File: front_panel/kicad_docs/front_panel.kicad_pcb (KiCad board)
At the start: 2 copper layers, 60.6 x 128.5 mm, 4 parts

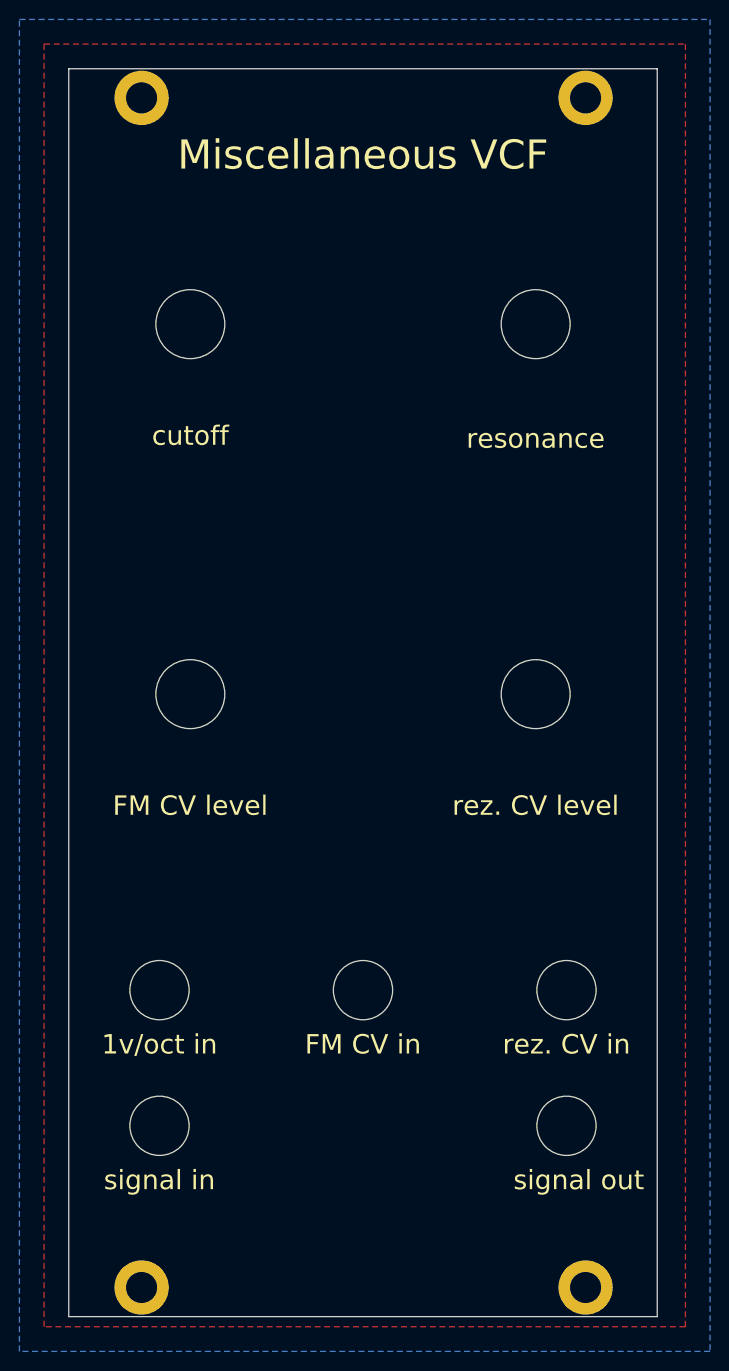
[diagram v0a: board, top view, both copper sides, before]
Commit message: fix misplaced headers, update readme
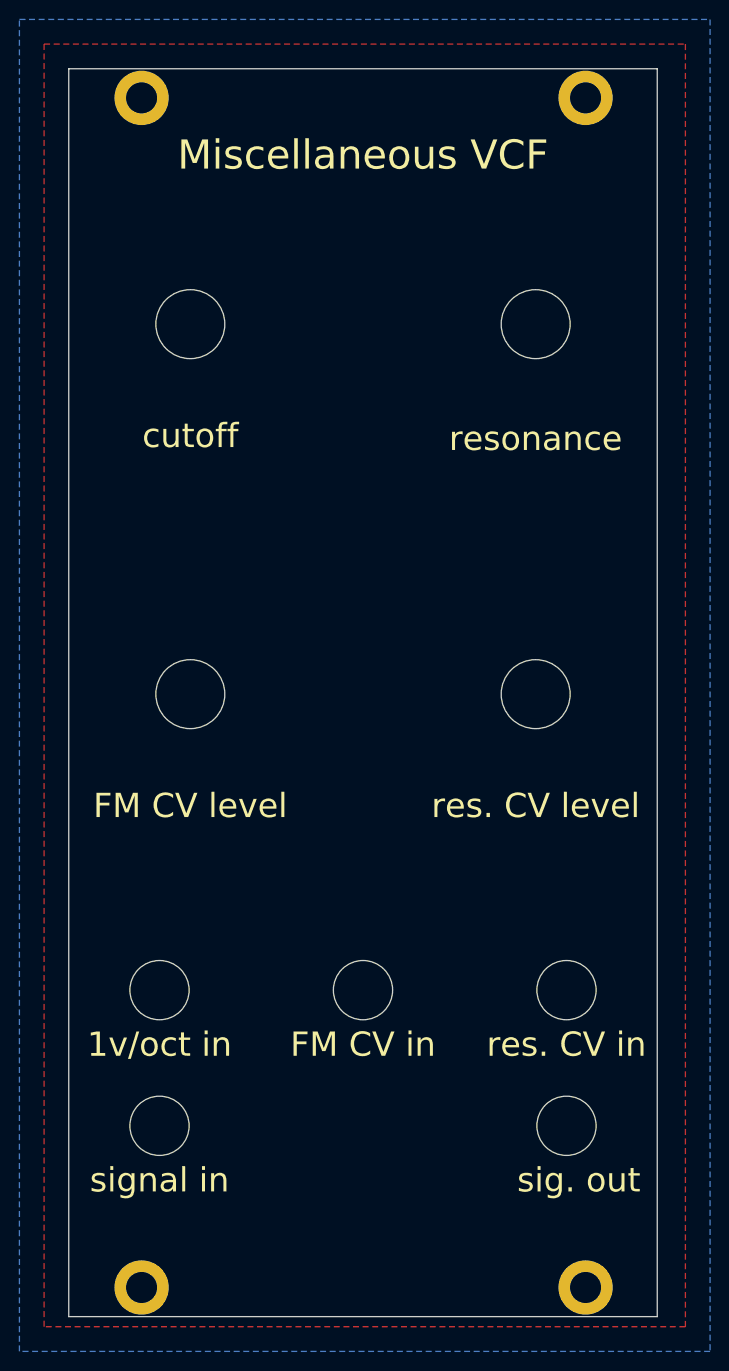
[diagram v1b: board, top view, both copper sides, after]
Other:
- board text added: "res. CV in"
- board text added: "res. CV level"
- board text added: "sig. out"
- board text removed: "rez. CV in"
- board text removed: "rez. CV level"
- board text removed: "signal out"
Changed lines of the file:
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@@
     (visible_elements FFFFFF7F)
     (pcbplotparams
-      (layerselection 0x010fc_ffffffff)
+      (layerselection 0x010f0_ffffffff)
       (usegerberextensions false)
       (usegerberattributes true)
       (usegerberadvancedattributes true)
-      (creategerberjobfile true)
+      (creategerberjobfile false)
       (excludeedgelayer true)
       (linewidth 0.100000)
@@
       (outputformat 1)
       (mirror false)
-      (drillshape 1)
+      (drillshape 0)
       (scaleselection 1)
-      (outputdirectory ""))
+      (outputdirectory "../construction_docs/gerbers/"))
   )
   (net 0 "")
@@
       (effects (font (size 1 1) (thickness 0.15)))
     )
+    (fp_circle (center 0 0) (end 2.8 0) (layer Cmts.User) (width 0.15))
+    (fp_circle (center 0 0) (end 3.05 0) (layer F.CrtYd) (width 0.05))
     (fp_text user %R (at 0.3 0) (layer F.Fab)
       (effects (font (size 1 1) (thickness 0.15)))
     )
-    (fp_circle (center 0 0) (end 2.8 0) (layer Cmts.User) (width 0.15))
-    (fp_circle (center 0 0) (end 3.05 0) (layer F.CrtYd) (width 0.05))
     (pad 1 thru_hole circle (at 0 0) (size 5.6 5.6) (drill 3.2) (layers *.Cu *.Mask)
       (net 1 GND))
@@
       (effects (font (size 1 1) (thickness 0.15)))
     )
+    (fp_circle (center 0 0) (end 2.8 0) (layer Cmts.User) (width 0.15))
+    (fp_circle (center 0 0) (end 3.05 0) (layer F.CrtYd) (width 0.05))
     (fp_text user %R (at 0.3 0) (layer F.Fab)
       (effects (font (size 1 1) (thickness 0.15)))
     )
-    (fp_circle (center 0 0) (end 2.8 0) (layer Cmts.User) (width 0.15))
-    (fp_circle (center 0 0) (end 3.05 0) (layer F.CrtYd) (width 0.05))
     (pad 1 thru_hole circle (at 0 0) (size 5.6 5.6) (drill 3.2) (layers *.Cu *.Mask)
       (net 1 GND))
@@
       (effects (font (size 1 1) (thickness 0.15)))
     )
+    (fp_circle (center 0 0) (end 2.8 0) (layer Cmts.User) (width 0.15))
+    (fp_circle (center 0 0) (end 3.05 0) (layer F.CrtYd) (width 0.05))
     (fp_text user %R (at 0.3 0) (layer F.Fab)
       (effects (font (size 1 1) (thickness 0.15)))
     )
-    (fp_circle (center 0 0) (end 2.8 0) (layer Cmts.User) (width 0.15))
-    (fp_circle (center 0 0) (end 3.05 0) (layer F.CrtYd) (width 0.05))
     (pad 1 thru_hole circle (at 0 0) (size 5.6 5.6) (drill 3.2) (layers *.Cu *.Mask)
       (net 1 GND))
@@
       (effects (font (size 1 1) (thickness 0.15)))
     )
+    (fp_circle (center 0 0) (end 2.8 0) (layer Cmts.User) (width 0.15))
+    (fp_circle (center 0 0) (end 3.05 0) (layer F.CrtYd) (width 0.05))
     (fp_text user %R (at 0.3 0) (layer F.Fab)
       (effects (font (size 1 1) (thickness 0.15)))
     )
-    (fp_circle (center 0 0) (end 2.8 0) (layer Cmts.User) (width 0.15))
-    (fp_circle (center 0 0) (end 3.05 0) (layer F.CrtYd) (width 0.05))
     (pad 1 thru_hole circle (at 0 0) (size 5.6 5.6) (drill 3.2) (layers *.Cu *.Mask)
       (net 1 GND))
   )
   (gr_text JLCJLCJLCJLC (at 30.3 2.54) (layer B.SilkS)
-    (effects (font (size 1 1) (thickness 0.15)) (justify mirror))
+    (effects (font (size 1.5 1.5) (thickness 0.2)) (justify mirror))
   )
   (gr_line (start 46.655 113.45) (end 55.855 113.45) (layer Dwgs.User) (width 0.15))
@@
   )
   (gr_text resonance (at 48.08 38.1) (layer F.SilkS)
-    (effects (font (size 2 2) (thickness 0.3)))
+    (effects (font (size 2.5 2.5) (thickness 0.3)))
   )
   (gr_text cutoff (at 12.52 37.8) (layer F.SilkS)
-    (effects (font (size 2 2) (thickness 0.3)))
+    (effects (font (size 2.5 2.5) (thickness 0.3)))
   )
-  (gr_text "rez. CV level" (at 48.08 75.9) (layer F.SilkS)
-    (effects (font (size 2 2) (thickness 0.3)))
+  (gr_text "res. CV level" (at 48.08 75.9) (layer F.SilkS)
+    (effects (font (size 2.5 2.5) (thickness 0.3)))
   )
   (gr_text "FM CV level" (at 12.52 75.9) (layer F.SilkS)
-    (effects (font (size 2 2) (thickness 0.3)))
+    (effects (font (size 2.5 2.5) (thickness 0.3)))
   )
-  (gr_text "signal out" (at 52.525 114.45) (layer F.SilkS)
-    (effects (font (size 2 2) (thickness 0.3)))
+  (gr_text "sig. out" (at 52.525 114.45) (layer F.SilkS)
+    (effects (font (size 2.5 2.5) (thickness 0.3)))
   )
   (gr_text "signal in" (at 9.345 114.45) (layer F.SilkS)
-    (effects (font (size 2 2) (thickness 0.3)))
+    (effects (font (size 2.5 2.5) (thickness 0.3)))
   )
-  (gr_text "rez. CV in" (at 51.255 100.48) (layer F.SilkS)
-    (effects (font (size 2 2) (thickness 0.3)))
+  (gr_text "res. CV in" (at 51.255 100.48) (layer F.SilkS)
+    (effects (font (size 2.5 2.5) (thickness 0.3)))
   )
   (gr_text "FM CV in" (at 30.3 100.48) (layer F.SilkS)
-    (effects (font (size 2 2) (thickness 0.3)))
+    (effects (font (size 2.5 2.5) (thickness 0.3)))
   )
   (gr_text "1v/oct in" (at 9.345 100.48) (layer F.SilkS)
-    (effects (font (size 2 2) (thickness 0.3)))
+    (effects (font (size 2.5 2.5) (thickness 0.3)))
   )
   (gr_circle (center 48.08 26.3) (end 54.43 26.3) (layer Dwgs.User) (width 0.15))
